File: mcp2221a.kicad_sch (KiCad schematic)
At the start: 58 parts, among them J401 Conn_01x04, J402 Conn_02x04_Odd_Even, J403 Barrel_Jack_Switch, J404 Conn_01x02, J405 Conn_01x02, J406 Conn_01x02, J407 Conn_01x02, J408 Conn_01x04, J409 Conn_01x06, K401 G5LE-1, Q401 DMG3414U, Q402 AO3401A, Q403 AO3401A, Q404 AO3401A, U402 MAX232, U403 PCF8574, U404 PC817, U405 PC817, U406 PC817, U407 PC817, U408 LM75B, U409 DS1307+, Y401 Crystal

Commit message: Add i2c_sampler, update to revision 3
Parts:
- removed C401: 1uF, Capacitor_SMD:C_0805_2012Metric_Pad1.18x1.45mm_HandSolder, symbol Device:C
- removed C402, C403, C404, C405: 1uF, Capacitor_SMD:C_0805_2012Metric_Pad1.15x1.40mm_HandSolder, symbol Device:C
- removed D401, D403, D404, D405: LED, LED_SMD:LED_0603_1608Metric_Pad1.05x0.95mm_HandSolder, symbol Device:LED
- removed D402: D, Diode_THT:D_DO-35_SOD27_P2.54mm_Vertical_AnodeUp, symbol Device:D
- removed J401: Conn_01x04, Connector_PinHeader_2.54mm:PinHeader_1x04_P2.54mm_Horizontal, symbol Connector_Generic:Conn_01x04
- removed J402: Conn_02x04_Odd_Even, Connector_PinHeader_2.54mm:PinHeader_2x04_P2.54mm_Vertical, symbol Connector_Generic:Conn_02x04_Odd_Even
- removed J403: Barrel_Jack_Switch, Connector_BarrelJack:BarrelJack_Horizontal, symbol Connector:Barrel_Jack_Switch
- removed J404, J405, J406, J407: Conn_01x02, TerminalBlock:TerminalBlock_bornier-2_P5.08mm, symbol Connector_Generic:Conn_01x02
- removed J408: Conn_01x04, Connector_PinHeader_2.54mm:PinHeader_1x04_P2.54mm_Vertical, symbol Connector_Generic:Conn_01x04
- removed J409: Conn_01x06, Connector_PinHeader_2.54mm:PinHeader_1x06_P2.54mm_Horizontal, symbol Connector_Generic:Conn_01x06
- removed JP401, JP402, JP403: Jumper, Resistor_SMD:R_1206_3216Metric, symbol iotether-rescue:Jumper-Device
- removed K401: G5LE-1, Relay_THT:Relay_SPDT_Omron-G5LE-1, symbol Relay:G5LE-1
- removed Q401: DMG3414U, Package_TO_SOT_SMD:SOT-23, symbol Transistor_FET:DMG3414U
- removed Q402, Q403, Q404: AO3401A, Package_TO_SOT_SMD:SOT-23, symbol Transistor_FET:AO3401A
- removed R401: 47k, Resistor_SMD:R_0603_1608Metric_Pad1.05x0.95mm_HandSolder, symbol Device:R
- removed R402, R403: 2.2k, Resistor_SMD:R_0603_1608Metric_Pad1.05x0.95mm_HandSolder, symbol Device:R
- removed R404, R413, R414, R415: 470, Resistor_SMD:R_0603_1608Metric_Pad1.05x0.95mm_HandSolder, symbol Device:R
- removed R405, R410, R411, R412: 1k, Resistor_SMD:R_0603_1608Metric_Pad1.05x0.95mm_HandSolder, symbol Device:R
- removed R406, R407, R408, R409: 100k, Resistor_SMD:R_0603_1608Metric_Pad1.05x0.95mm_HandSolder, symbol Device:R
- removed RN401: 220, Resistor_THT:R_Array_SIP5, symbol Device:R_Network04
- removed U401: (no value), symbol iotether-rescue:MCP2221AxSL-Interface_USB
- removed U402: MAX232, Package_DIP:DIP-16_W7.62mm_Socket, symbol Interface_UART:MAX232
- removed U403: PCF8574, Package_SO:SOIC-16W_7.5x10.3mm_P1.27mm, symbol Interface_Expansion:PCF8574
- removed U404, U405, U406, U407: PC817, Package_DIP:DIP-4_W7.62mm, symbol Isolator:PC817
- added C309, C310: 22pf, Capacitor_SMD:C_0805_2012Metric_Pad1.18x1.45mm_HandSolder, symbol Device:C
- added C311: C, Capacitor_SMD:C_0603_1608Metric_Pad1.08x0.95mm_HandSolder, symbol Device:C
- added C312: .1uf, Capacitor_SMD:C_0603_1608Metric_Pad1.08x0.95mm_HandSolder, symbol Device:C
- added C313, C314, C315, C316: C, Capacitor_SMD:C_0805_2012Metric_Pad1.18x1.45mm_HandSolder, symbol Device:C
- added J305: Conn_02x04_Odd_Even, Connector_PinHeader_2.54mm:PinHeader_2x04_P2.54mm_Vertical, symbol Connector_Generic:Conn_02x04_Odd_Even
- added J306, J307: Conn_01x09, Connector_USB:USB_A_Wuerth_61400826021_Horizontal_Stacked, symbol Connector_Generic:Conn_01x09
- added R307, R308, R309, R310, R311, R314, R315, R316, R318, R319: R, Resistor_SMD:R_0603_1608Metric_Pad0.98x0.95mm_HandSolder, symbol Device:R
- added R312, R313: 2.2k, Resistor_SMD:R_0603_1608Metric_Pad0.98x0.95mm_HandSolder, symbol Device:R
- added R317: 15k, Resistor_SMD:R_0603_1608Metric_Pad0.98x0.95mm_HandSolder, symbol Device:R
- added SW301, SW302, SW303, SW304: SW_Push, Button_Switch_THT:SW_PUSH_6mm, symbol Switch:SW_Push
- added U303: ATmega328P-P, Package_DIP:DIP-28_W7.62mm, symbol MCU_Microchip_ATmega:ATmega328P-P
- added U304: FE1.1s, Package_SO:SSOP-28_3.9x9.9mm_P0.635mm, symbol Interface_USB:FE1.1s
- added Y302, Y303: Crystal, Crystal:Crystal_HC49-U_Vertical, symbol Device:Crystal
- C406, C407: footprint Capacitor_SMD:C_0603_1608Metric_Pad1.05x0.95mm_HandSolder -> Capacitor_SMD:C_0603_1608Metric_Pad1.08x0.95mm_HandSolder
- R416: footprint Resistor_SMD:R_0603_1608Metric_Pad1.05x0.95mm_HandSolder -> Resistor_SMD:R_0603_1608Metric_Pad0.98x0.95mm_HandSolder
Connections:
- net +5V: now also J305.1 (Pin_1), J305.2 (Pin_2), J306.1 (Pin_1), J306.5 (Pin_5), J307.1 (Pin_1), J307.5 (Pin_5), R307.1, R308.1, R310.1, R312.1, R313.1, R314.1, R315.1, R316.1, R317.1, R318.1, U303.20 (AVCC), U303.7 (VCC), U304.20 (VDD5)
- net GND: now also C309.2, C310.2, C312.2, C313.2, C314.2, C315.2, C316.2, J305.7 (Pin_7), J305.8 (Pin_8), J306.4 (Pin_4), J306.8 (Pin_8), J306.9 (Pin_9), J307.4 (Pin_4), J307.8 (Pin_8), J307.9 (Pin_9), R319.2, SW301.1, SW302.1, SW303.1, SW304.1, U303.22 (GND), U303.8 (GND), U304.1 (VSS)
- net SCL: now also J305.5 (Pin_5), J305.6 (Pin_6), R313.2, U303.28 (PC5)
- net SDA: now also J305.3 (Pin_3), J305.4 (Pin_4), R312.2, U303.27 (PC4)
- net U_MCP+: now also U304.16 (DPU)
- net U_MCP-: now also U304.15 (DMU)
- new net: R310.2, R311.1, U303.2 (PD0)
- new net: C309.1, U303.10 (XTAL2/PB7), Y302.1
- new net: R319.1, U304.14 (REXT)
- new net: R318.2, U304.18 (VBUSM)
- new net: C310.1, U303.9 (XTAL1/PB6), Y302.2
- new net: C315.1, U304.3 (XIN), Y303.1
- new net: C316.1, U304.2 (XOUT), Y303.2
- new net: J307.2 (Pin_2), U304.6 (DM3)
- new net: J307.3 (Pin_3), U304.7 (DP3)
- new net: J307.6 (Pin_6), U304.4 (DM4)
- new net: J307.7 (Pin_7), U304.5 (DP4)
- new net: R308.2, R309.1, U303.3 (PD1)
- new net: C314.1, U304.13 (VD33), U304.21 (VD33_O)
- new net: C312.1, R317.2, U304.17 (~{XRSTJ}), U304.19 (BUSJ), U304.26 (OVCJ)
- new net: J306.2 (Pin_2), U304.10 (DM1)
- new net: J306.3 (Pin_3), U304.11 (DP1)
- new net: C313.1, U304.12 (VD18_O), U304.28 (VD18)
- new net: J306.6 (Pin_6), U304.8 (DM2)
- new net: J306.7 (Pin_7), U304.9 (DP2)
- new net ATM_DTR: C311.2
- new net ATM_RESET: C311.1, R307.2, SW301.2, U303.1 (~{RESET}/PC6)
- new net ATM_RX: R311.2
- new net ATM_TX: R309.2
- new net IN0: R314.2, SW302.2, U303.11 (PD5)
- new net IN1: R315.2, SW303.2, U303.12 (PD6)
- new net IN2: R316.2, SW304.2, U303.13 (PD7)
- new net SW0: U303.6 (PD4)
- new net SW1: U303.4 (PD2)

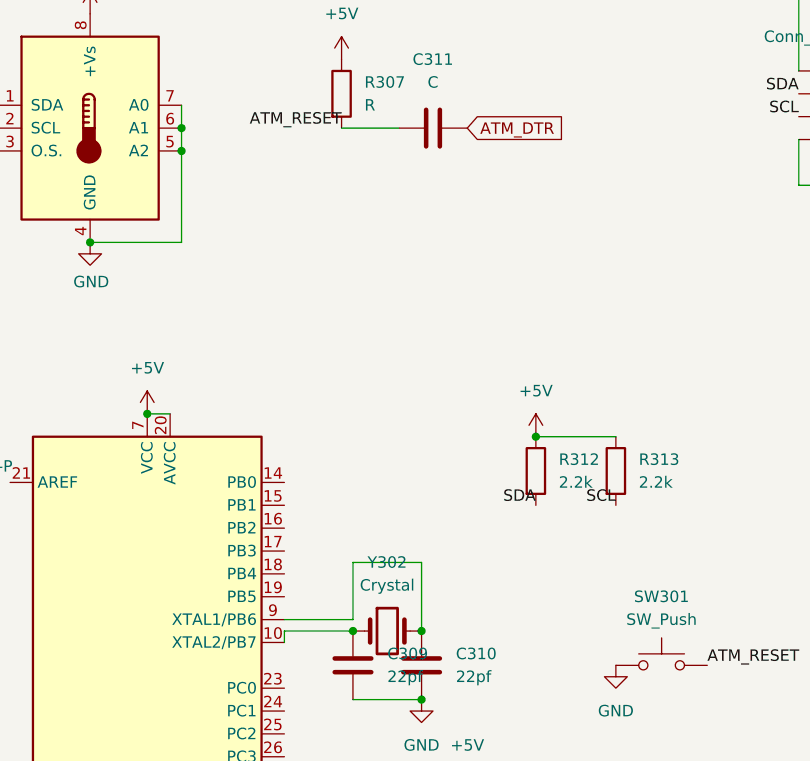
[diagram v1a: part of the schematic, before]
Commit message: Add 12V->5V regulator
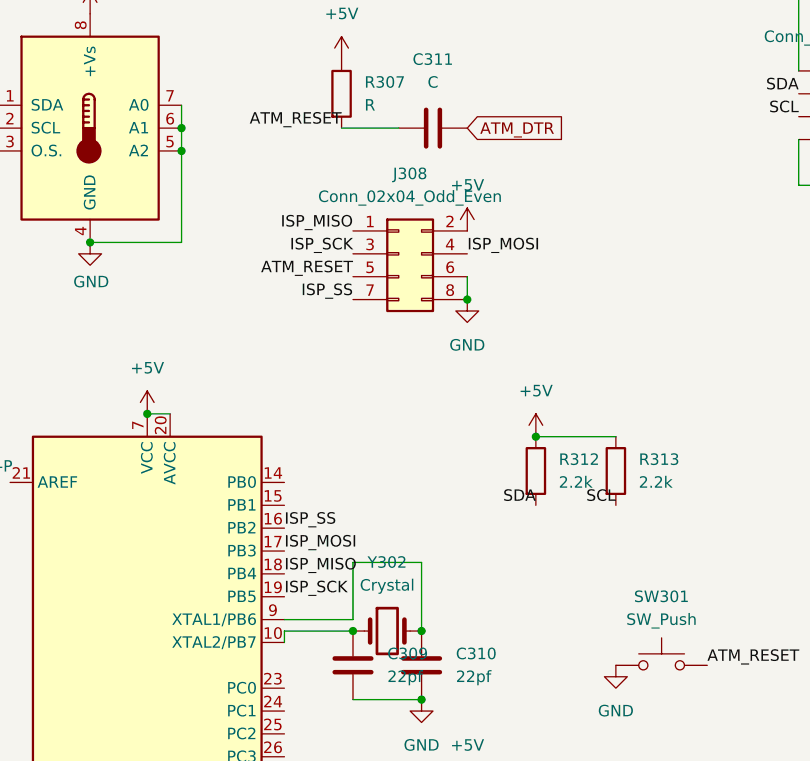
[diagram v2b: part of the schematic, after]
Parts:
- added J308: Conn_02x04_Odd_Even, Connector_PinHeader_2.54mm:PinHeader_2x04_P2.54mm_Vertical, symbol Connector_Generic:Conn_02x04_Odd_Even
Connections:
- net +5V: now also J308.2 (Pin_2)
- net ATM_RESET: now also J308.5 (Pin_5)
- net GND: now also J308.6 (Pin_6), J308.8 (Pin_8)
- net ISP_SS: now reaches U303.16 (PB2)
- net ISP_SS: now also J308.7 (Pin_7)
- net ISP_MOSI: now reaches U303.17 (PB3)
- net ISP_MOSI: now also J308.4 (Pin_4)
- net ISP_MISO: now reaches U303.18 (PB4)
- net ISP_MISO: now also J308.1 (Pin_1)
- net ISP_SCK: now reaches U303.19 (PB5)
- net ISP_SCK: now also J308.3 (Pin_3)
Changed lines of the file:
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@@
   (junction (at 68.58 135.89) (diameter 0) (color 0 0 0 0)
   )
+  (junction (at 73.66 99.06) (diameter 0) (color 0 0 0 0)
+  )
   (junction (at 68.58 143.51) (diameter 0) (color 0 0 0 0)
   )
@@
     (stroke (width 0) (type default) (color 0 0 0 0))
   )
+  (wire (pts (xy 73.66 96.52) (xy 73.66 99.06))
+    (stroke (width 0) (type default) (color 0 0 0 0))
+  )
   (wire (pts (xy 97.79 15.24) (xy 97.79 26.67))
     (stroke (width 0) (type default) (color 0 0 0 0))
@@
     (stroke (width 0) (type default) (color 0 0 0 0))
   )
+  (label "ISP_MISO" (at 53.34 129.54 0)
+    (effects (font (size 1.27 1.27)) (justify left bottom))
+  )
   (label "ATM_RESET" (at 59.69 80.01 180)
     (effects (font (size 1.27 1.27)) (justify right bottom))
   )
+  (label "ISP_SCK" (at 53.34 132.08 0)
+    (effects (font (size 1.27 1.27)) (justify left bottom))
+  )
   (label "SCL" (at 110.49 78.74 180)
     (effects (font (size 1.27 1.27)) (justify right bottom))
@@
     (effects (font (size 1.27 1.27)) (justify left bottom))
   )
+  (label "ISP_SCK" (at 60.96 93.98 180)
+    (effects (font (size 1.27 1.27)) (justify right bottom))
+  )
+  (label "ISP_SS" (at 53.34 124.46 0)
+    (effects (font (size 1.27 1.27)) (justify left bottom))
+  )
   (label "SCL" (at 85.09 31.75 180)
     (effects (font (size 1.27 1.27)) (justify right bottom))
@@
     (effects (font (size 1.27 1.27)) (justify right bottom))
   )
+  (label "ATM_RESET" (at 60.96 96.52 180)
+    (effects (font (size 1.27 1.27)) (justify right bottom))
+  )
   (label "IN0" (at 163.83 74.93 0)
     (effects (font (size 1.27 1.27)) (justify left bottom))
@@
     (effects (font (size 1.27 1.27)) (justify left bottom))
   )
+  (label "ISP_MOSI" (at 73.66 93.98 0)
+    (effects (font (size 1.27 1.27)) (justify left bottom))
+  )
   (label "IN1" (at 53.34 177.8 0)
     (effects (font (size 1.27 1.27)) (justify left bottom))
@@
     (effects (font (size 1.27 1.27)) (justify left bottom))
   )
+  (label "ISP_MISO" (at 60.96 91.44 180)
+    (effects (font (size 1.27 1.27)) (justify right bottom))
+  )
   (label "SDA" (at 53.34 152.4 0)
     (effects (font (size 1.27 1.27)) (justify left bottom))
@@
     (effects (font (size 1.27 1.27)) (justify right bottom))
   )
+  (label "ISP_MOSI" (at 53.34 127 0)
+    (effects (font (size 1.27 1.27)) (justify left bottom))
+  )
   (label "SDA" (at 110.49 76.2 180)
     (effects (font (size 1.27 1.27)) (justify right bottom))
@@
   )
   (label "SCL" (at 21.59 80.01 180)
+    (effects (font (size 1.27 1.27)) (justify right bottom))
+  )
+  (label "ISP_SS" (at 60.96 99.06 180)
     (effects (font (size 1.27 1.27)) (justify right bottom))
   )
@@
     (pin "2")
   )
+  (symbol (lib_id "power:+5V") (at 73.66 91.44 0) (unit 1)
+    (in_bom yes) (on_board yes) (fields_autoplaced)
+    (property "Reference" "#PWR0302" (id 0) (at 73.66 95.25 0)
+      (effects (font (size 1.27 1.27)) hide)
+    )
+    (property "Value" "+5V" (id 1) (at 73.66 86.36 0))
+    (property "Footprint" "" (id 2) (at 73.66 91.44 0)
+      (effects (font (size 1.27 1.27)) hide)
+    )
+    (property "Datasheet" "" (id 3) (at 73.66 91.44 0)
+      (effects (font (size 1.27 1.27)) hide)
+    )
+    (pin "1")
+  )
   (symbol (lib_id "power:GND") (at 265.43 49.53 0) (unit 1)
     (in_bom yes) (on_board yes) (fields_autoplaced)
@@
     (pin "2")
   )
+  (symbol (lib_id "power:GND") (at 73.66 99.06 0) (unit 1)
+    (in_bom yes) (on_board yes) (fields_autoplaced)
+    (property "Reference" "#PWR0303" (id 0) (at 73.66 105.41 0)
+      (effects (font (size 1.27 1.27)) hide)
+    )
+    (property "Value" "GND" (id 1) (at 73.66 104.14 0))
+    (property "Footprint" "" (id 2) (at 73.66 99.06 0)
+      (effects (font (size 1.27 1.27)) hide)
+    )
+    (property "Datasheet" "" (id 3) (at 73.66 99.06 0)
+      (effects (font (size 1.27 1.27)) hide)
+    )
+    (pin "1")
+  )
   (symbol (lib_id "Device:R") (at 196.85 80.01 0) (unit 1)
     (in_bom yes) (on_board yes) (fields_autoplaced)
@@
     (pin "2")
   )
+  (symbol (lib_id "Connector_Generic:Conn_02x04_Odd_Even") (at 66.04 93.98 0) (unit 1)
+    (in_bom yes) (on_board yes) (fields_autoplaced)
+    (property "Reference" "J308" (id 0) (at 67.31 85.09 0))
+    (property "Value" "Conn_02x04_Odd_Even" (id 1) (at 67.31 87.63 0))
+    (property "Footprint" "Connector_PinHeader_2.54mm:PinHeader_2x04_P2.54mm_Vertical" (id 2) (at 66.04 93.98 0)
+      (effects (font (size 1.27 1.27)) hide)
+    )
+    (property "Datasheet" "~" (id 3) (at 66.04 93.98 0)
+      (effects (font (size 1.27 1.27)) hide)
+    )
+    (pin "1")
+    (pin "2")
+    (pin "3")
+    (pin "4")
+    (pin "5")
+    (pin "6")
+    (pin "7")
+    (pin "8")
+  )
   (symbol (lib_id "power:GND") (at 153.67 90.17 0) (unit 1)
